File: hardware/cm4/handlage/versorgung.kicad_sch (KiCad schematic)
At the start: 7 parts, among them J10 USB-C 5V/USB, U10 USBLC6-2SC6

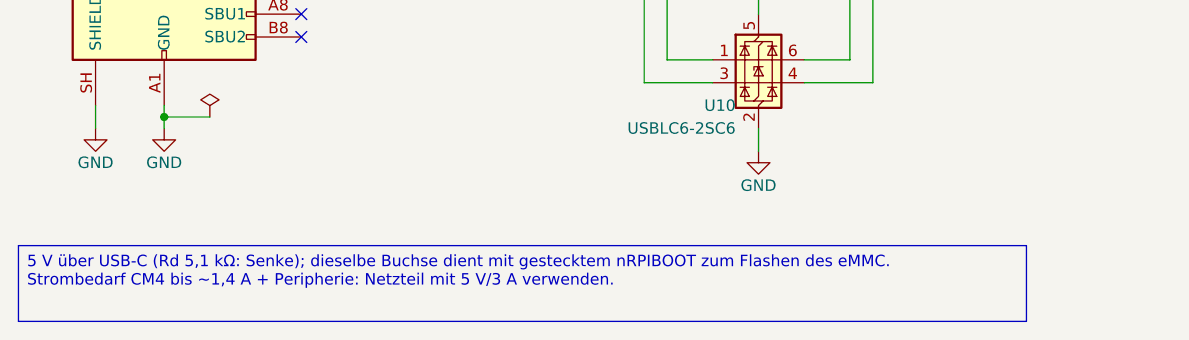
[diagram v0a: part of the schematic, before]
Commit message: CM4-Schaltplan: Handänderungen übernommen (Handlage für 8 Blätter, 2 Texte zurückgeführt); Kastenhöhen aus gemessenen Zeichenbreiten
Co-Authored-By: Claude Opus 5.5 <noreply@anthropic.com>
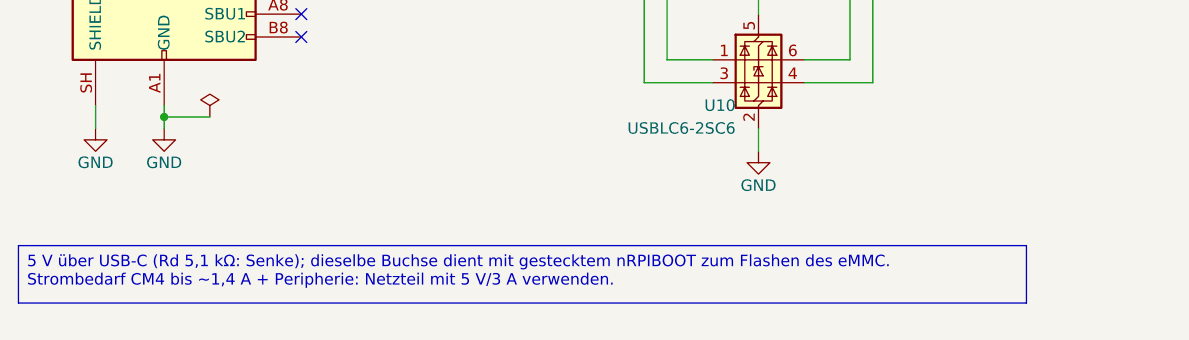
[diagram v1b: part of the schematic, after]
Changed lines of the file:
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@@
 		)
 	)
-(text_box "5 V über USB-C (Rd 5,1 kΩ: Senke); dieselbe Buchse dient mit gestecktem nRPIBOOT zum Flashen des eMMC.\nStrombedarf CM4 bis ~1,4 A + Peripherie: Netzteil mit 5 V/3 A verwenden." (exclude_from_sim no) (at 132.4 159.07 0) (size 112 8.42) (margins 0.9525 0.9525 0.9525 0.9525) (stroke (width 0.1) (type solid) (color 132 132 132 1)) (fill (type color) (color 255 255 230 1)) (effects (font (size 1.27 1.27)) (justify left top)))
+(text_box "5 V über USB-C (Rd 5,1 kΩ: Senke); dieselbe Buchse dient mit gestecktem nRPIBOOT zum Flashen des eMMC.\nStrombedarf CM4 bis ~1,4 A + Peripherie: Netzteil mit 5 V/3 A verwenden." (exclude_from_sim no) (at 132.4 159.07 0) (size 112 6.38) (margins 0.9525 0.9525 0.9525 0.9525) (stroke (width 0.1) (type solid) (color 132 132 132 1)) (fill (type color) (color 255 255 230 1)) (effects (font (size 1.27 1.27)) (justify left top)))
 	)
